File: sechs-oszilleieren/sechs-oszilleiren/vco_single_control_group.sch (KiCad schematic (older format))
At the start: 6 parts

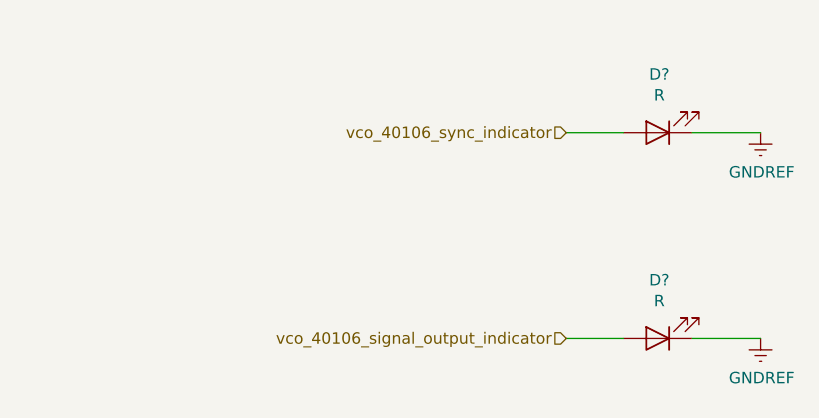
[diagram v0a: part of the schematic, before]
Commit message: Rearranged labeling on voice board, simplified output stage and reduced part count. Simplified CD40106 feedback nets.
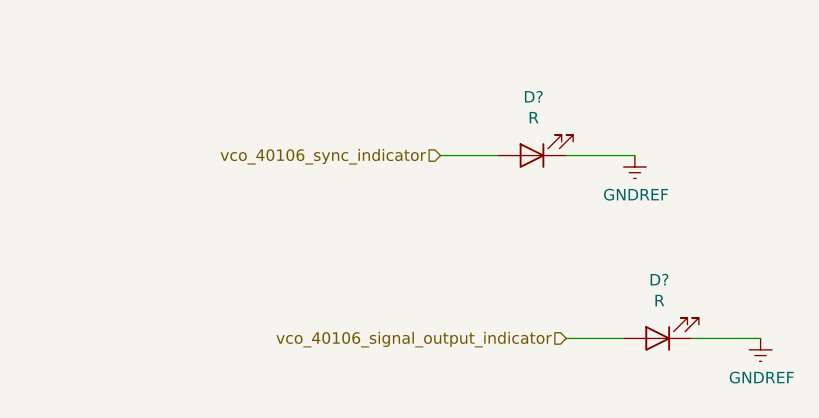
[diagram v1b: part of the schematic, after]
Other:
- moved on the sheet: D?
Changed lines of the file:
@@
 $Descr USLetter 11000 8500
 encoding utf-8
-Sheet 4 12
+Sheet 6 11
 Title "Sechs-Oszilléierer"
 Date "2020-04-04"
@@
 AR Path="/5E724F09/5E8AD743/5E8E3E2E/5E8AEA40" Ref="RV?"  Part="1"
 AR Path="/5E724F09/5E8AD743/5E8E5E8A/5E8AEA40" Ref="RV?"  Part="1"
+AR Path="/5E724F09/5E8AD743/5E917CFD/5E8AEA40" Ref="RV?"  Part="1"
+AR Path="/5E724F09/5E8AD743/5E917D27/5E8AEA40" Ref="RV?"  Part="1"
+AR Path="/5E724F09/5E8AD743/5E917D70/5E8AEA40" Ref="RV?"  Part="1"
 F 0 "RV?" H 3481 2446 50  0000 R CNN
 F 1 "10K" H 3481 2355 50  0000 R CNN
@@
 AR Path="/5E724F09/5E8AD743/5E8E3E2E/5E8B2987" Ref="J?"  Part="1"
 AR Path="/5E724F09/5E8AD743/5E8E5E8A/5E8B2987" Ref="J?"  Part="1"
+AR Path="/5E724F09/5E8AD743/5E917CFD/5E8B2987" Ref="J?"  Part="1"
+AR Path="/5E724F09/5E8AD743/5E917D27/5E8B2987" Ref="J?"  Part="1"
+AR Path="/5E724F09/5E8AD743/5E917D70/5E8B2987" Ref="J?"  Part="1"
 F 0 "J?" H 6782 5225 50  0000 C CNN
 F 1 "sync_in" H 6782 5134 50  0000 C CNN
@@
 AR Path="/5E724F09/5E8AD743/5E8E3E2E/5E8B3E62" Ref="J?"  Part="1"
 AR Path="/5E724F09/5E8AD743/5E8E5E8A/5E8B3E62" Ref="J?"  Part="1"
+AR Path="/5E724F09/5E8AD743/5E917CFD/5E8B3E62" Ref="J?"  Part="1"
+AR Path="/5E724F09/5E8AD743/5E917D27/5E8B3E62" Ref="J?"  Part="1"
+AR Path="/5E724F09/5E8AD743/5E917D70/5E8B3E62" Ref="J?"  Part="1"
 F 0 "J?" H 2082 5175 50  0000 C CNN
 F 1 "cv_in" H 2082 5084 50  0000 C CNN
@@
 	1    0    0    1
 $EndComp
-$Comp
-L Device:LED D?
-U 1 1 5E8B6EB1
-P 8500 1950
-AR Path="/5E724F09/5E8AD743/5E8AE40B/5E8B6EB1" Ref="D?"  Part="1"
-AR Path="/5E724F09/5E8AD743/5E8DD50C/5E8B6EB1" Ref="D?"  Part="1"
-AR Path="/5E724F09/5E8AD743/5E8DD766/5E8B6EB1" Ref="D?"  Part="1"
-AR Path="/5E724F09/5E8AD743/5E8E3E2E/5E8B6EB1" Ref="D?"  Part="1"
-AR Path="/5E724F09/5E8AD743/5E8E5E8A/5E8B6EB1" Ref="D?"  Part="1"
-F 0 "D?" H 8493 1695 50  0000 C CNN
-F 1 "R" H 8493 1786 50  0000 C CNN
-F 2 "LED_THT:LED_D3.0mm" H 8500 1950 50  0001 C CNN
-F 3 "~" H 8500 1950 50  0001 C CNN
-	1    8500 1950
-	-1   0    0    1
-$EndComp
-Wire Wire Line
-	8350 1950 8100 1950
-Wire Wire Line
-	8650 1950 8950 1950
-$Comp
-L power:GNDREF #PWR?
-U 1 1 5E8BFD97
-P 8950 1950
-AR Path="/5E724F09/5E8AD743/5E8AE40B/5E8BFD97" Ref="#PWR?"  Part="1"
-AR Path="/5E724F09/5E8AD743/5E8DD50C/5E8BFD97" Ref="#PWR?"  Part="1"
-AR Path="/5E724F09/5E8AD743/5E8DD766/5E8BFD97" Ref="#PWR?"  Part="1"
-AR Path="/5E724F09/5E8AD743/5E8E3E2E/5E8BFD97" Ref="#PWR?"  Part="1"
-AR Path="/5E724F09/5E8AD743/5E8E5E8A/5E8BFD97" Ref="#PWR?"  Part="1"
-F 0 "#PWR?" H 8950 1700 50  0001 C CNN
-F 1 "GNDREF" H 8955 1777 50  0000 C CNN
-F 2 "" H 8950 1950 50  0001 C CNN
-F 3 "" H 8950 1950 50  0001 C CNN
-	1    8950 1950
-	1    0    0    -1
-$EndComp
-Text HLabel 8100 1950 0    50   Input ~ 0
-vco_40106_sync_indicator
 $Comp
 L Device:LED D?
@@
 AR Path="/5E724F09/5E8AD743/5E8E3E2E/5E8C0E60" Ref="D?"  Part="1"
 AR Path="/5E724F09/5E8AD743/5E8E5E8A/5E8C0E60" Ref="D?"  Part="1"
+AR Path="/5E724F09/5E8AD743/5E917CFD/5E8C0E60" Ref="D?"  Part="1"
+AR Path="/5E724F09/5E8AD743/5E917D27/5E8C0E60" Ref="D?"  Part="1"
+AR Path="/5E724F09/5E8AD743/5E917D70/5E8C0E60" Ref="D?"  Part="1"
 F 0 "D?" H 8493 2595 50  0000 C CNN
 F 1 "R" H 8493 2686 50  0000 C CNN
@@
 AR Path="/5E724F09/5E8AD743/5E8E3E2E/5E8C0E6C" Ref="#PWR?"  Part="1"
 AR Path="/5E724F09/5E8AD743/5E8E5E8A/5E8C0E6C" Ref="#PWR?"  Part="1"
+AR Path="/5E724F09/5E8AD743/5E917CFD/5E8C0E6C" Ref="#PWR?"  Part="1"
+AR Path="/5E724F09/5E8AD743/5E917D27/5E8C0E6C" Ref="#PWR?"  Part="1"
+AR Path="/5E724F09/5E8AD743/5E917D70/5E8C0E6C" Ref="#PWR?"  Part="1"
 F 0 "#PWR?" H 8950 2600 50  0001 C CNN
 F 1 "GNDREF" H 8955 2677 50  0000 C CNN
@@
 AR Path="/5E724F09/5E8AD743/5E8E3E2E/5E8C41EA" Ref="SW?"  Part="1"
 AR Path="/5E724F09/5E8AD743/5E8E5E8A/5E8C41EA" Ref="SW?"  Part="1"
+AR Path="/5E724F09/5E8AD743/5E917CFD/5E8C41EA" Ref="SW?"  Part="1"
+AR Path="/5E724F09/5E8AD743/5E917D27/5E8C41EA" Ref="SW?"  Part="1"
+AR Path="/5E724F09/5E8AD743/5E917D70/5E8C41EA" Ref="SW?"  Part="1"
 F 0 "SW?" V 2504 2098 50  0000 L CNN
 F 1 "wave_shape_select" V 2595 2098 50  0000 L CNN
@@
 Wire Wire Line
 	2450 2350 2200 2350
-Wire Wire Line
-	2200 3200 2650 3200
 Connection ~ 3550 3200
 Wire Wire Line
 	2650 2150 2650 3200
-Connection ~ 2650 3200
 Wire Wire Line
 	2650 3200 3550 3200
@@
 Connection ~ 3550 1500
 Text HLabel 2200 2350 0    50   Output ~ 0
-vco_40106_diode
-Text HLabel 2200 3200 0    50   Input ~ 0
 vco_40106_diode
 Wire Wire Line
@@
 AR Path="/5E724F09/5E8AD743/5E8E3E2E/5E8D6EF9" Ref="#PWR?"  Part="1"
 AR Path="/5E724F09/5E8AD743/5E8E5E8A/5E8D6EF9" Ref="#PWR?"  Part="1"
+AR Path="/5E724F09/5E8AD743/5E917CFD/5E8D6EF9" Ref="#PWR?"  Part="1"
+AR Path="/5E724F09/5E8AD743/5E917D27/5E8D6EF9" Ref="#PWR?"  Part="1"
+AR Path="/5E724F09/5E8AD743/5E917D70/5E8D6EF9" Ref="#PWR?"  Part="1"
 F 0 "#PWR?" H 7100 4950 50  0001 C CNN
 F 1 "GNDREF" H 7105 5027 50  0000 C CNN
@@
 AR Path="/5E724F09/5E8AD743/5E8E3E2E/5E8D7CC6" Ref="#PWR?"  Part="1"
 AR Path="/5E724F09/5E8AD743/5E8E5E8A/5E8D7CC6" Ref="#PWR?"  Part="1"
+AR Path="/5E724F09/5E8AD743/5E917CFD/5E8D7CC6" Ref="#PWR?"  Part="1"
+AR Path="/5E724F09/5E8AD743/5E917D27/5E8D7CC6" Ref="#PWR?"  Part="1"
+AR Path="/5E724F09/5E8AD743/5E917D70/5E8D7CC6" Ref="#PWR?"  Part="1"
 F 0 "#PWR?" H 2550 4900 50  0001 C CNN
 F 1 "GNDREF" H 2555 4977 50  0000 C CNN
@@
 Text HLabel 2750 4850 2    50   Output ~ 0
 vco_40106_cv
+Text HLabel 2550 4400 1    50   Input ~ 0
+internal_cv
+Wire Wire Line
+	2550 4400 2550 4750
 Text HLabel 7100 4450 1    50   UnSpc ~ 0
 pulldown_r
 Text HLabel 7500 4900 2    50   Output ~ 0
 vco_40106_sync
-Text HLabel 2550 4400 1    50   Input ~ 0
-internal_cv
-Wire Wire Line
-	2550 4400 2550 4750
+Connection ~ 2650 3200
+Wire Wire Line
+	2200 3200 2650 3200
+Text HLabel 2200 3200 0    50   Input ~ 0
+vco_40106_diode
+Text HLabel 7550 2050 0    50   Input ~ 0
+vco_40106_sync_indicator
+$Comp
+L power:GNDREF #PWR?
+U 1 1 5E8BFD97
+P 8400 2050
+AR Path="/5E724F09/5E8AD743/5E8AE40B/5E8BFD97" Ref="#PWR?"  Part="1"
+AR Path="/5E724F09/5E8AD743/5E8DD50C/5E8BFD97" Ref="#PWR?"  Part="1"
+AR Path="/5E724F09/5E8AD743/5E8DD766/5E8BFD97" Ref="#PWR?"  Part="1"
+AR Path="/5E724F09/5E8AD743/5E8E3E2E/5E8BFD97" Ref="#PWR?"  Part="1"
+AR Path="/5E724F09/5E8AD743/5E8E5E8A/5E8BFD97" Ref="#PWR?"  Part="1"
+AR Path="/5E724F09/5E8AD743/5E917CFD/5E8BFD97" Ref="#PWR?"  Part="1"
+AR Path="/5E724F09/5E8AD743/5E917D27/5E8BFD97" Ref="#PWR?"  Part="1"
+AR Path="/5E724F09/5E8AD743/5E917D70/5E8BFD97" Ref="#PWR?"  Part="1"
+F 0 "#PWR?" H 8400 1800 50  0001 C CNN
+F 1 "GNDREF" H 8405 1877 50  0000 C CNN
+F 2 "" H 8400 2050 50  0001 C CNN
+F 3 "" H 8400 2050 50  0001 C CNN
+	1    8400 2050
+	1    0    0    -1
+$EndComp
+Wire Wire Line
+	8100 2050 8400 2050
+Wire Wire Line
+	7800 2050 7550 2050
+$Comp
+L Device:LED D?
+U 1 1 5E8B6EB1
+P 7950 2050
+AR Path="/5E724F09/5E8AD743/5E8AE40B/5E8B6EB1" Ref="D?"  Part="1"
+AR Path="/5E724F09/5E8AD743/5E8DD50C/5E8B6EB1" Ref="D?"  Part="1"
+AR Path="/5E724F09/5E8AD743/5E8DD766/5E8B6EB1" Ref="D?"  Part="1"
+AR Path="/5E724F09/5E8AD743/5E8E3E2E/5E8B6EB1" Ref="D?"  Part="1"
+AR Path="/5E724F09/5E8AD743/5E8E5E8A/5E8B6EB1" Ref="D?"  Part="1"
+AR Path="/5E724F09/5E8AD743/5E917CFD/5E8B6EB1" Ref="D?"  Part="1"
+AR Path="/5E724F09/5E8AD743/5E917D27/5E8B6EB1" Ref="D?"  Part="1"
+AR Path="/5E724F09/5E8AD743/5E917D70/5E8B6EB1" Ref="D?"  Part="1"
+F 0 "D?" H 7943 1795 50  0000 C CNN
+F 1 "R" H 7943 1886 50  0000 C CNN
+F 2 "LED_THT:LED_D3.0mm" H 7950 2050 50  0001 C CNN
+F 3 "~" H 7950 2050 50  0001 C CNN
+	1    7950 2050
+	-1   0    0    1
+$EndComp
 $EndSCHEMATC
